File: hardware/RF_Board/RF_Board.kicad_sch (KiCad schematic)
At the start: 130 parts, among them J1 Conn_Coaxial, J2 Conn_01x04_Male, J3 Conn_Coaxial, J4 Conn_01x04_Male, J5 Conn_01x06_Female, J6 Conn_01x06_Female, J7 Conn_01x06_Female, J8 L77TSAH15SOL2RM8, Q1 2N7002, Q2 2N7002, U1 MSP430FR2355TPT, U10 QPL9096, U11 QPL9096, U12 74HC04, U13 RFM95PW, U14 TPS259573DSGR, U15 TPS259573DSGR, U2 MSP430FR2355TPT, U3 CC2500, U4 HMC574, U5 HMC574, U6 YAT-5A+, U7 SKY65900-11, U8 LFCN-2750+, U9 DEA202450BT-1213C1, Y1 Crystal_GND24, Y2 Crystal, Y3 Crystal

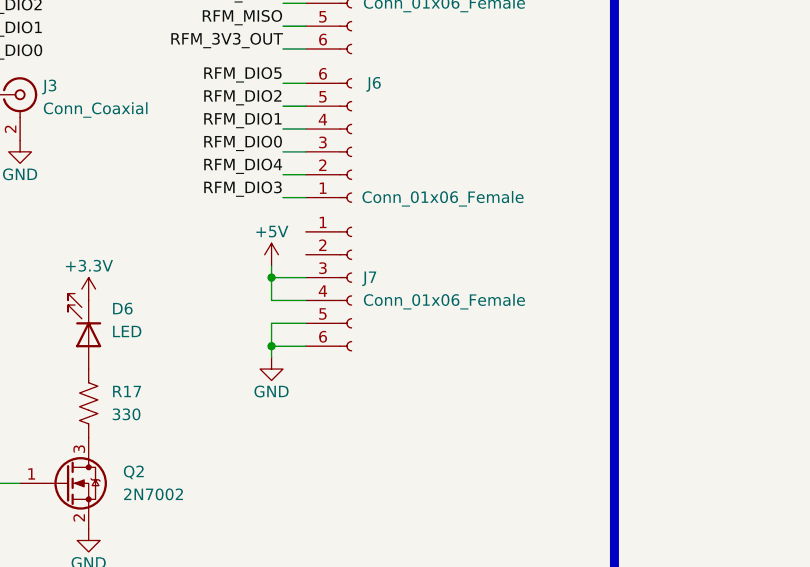
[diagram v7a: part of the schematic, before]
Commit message: start RF board digital routing
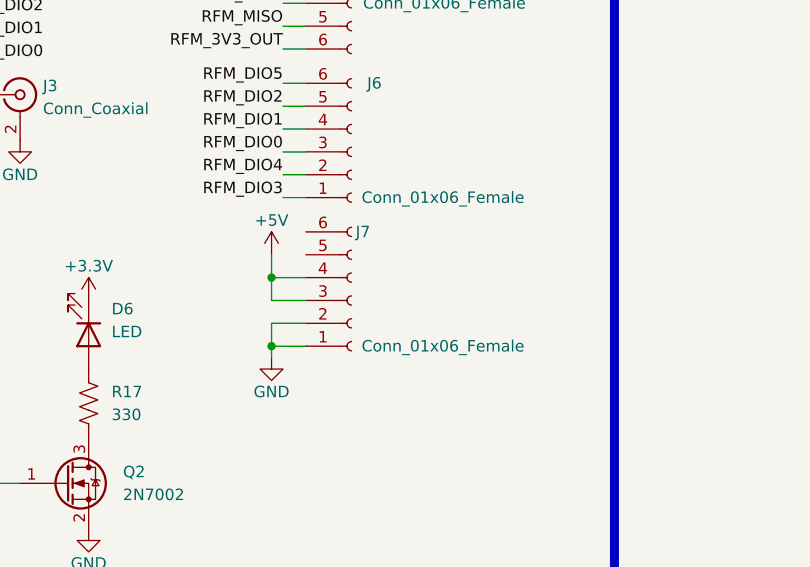
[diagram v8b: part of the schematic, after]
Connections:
- net GND: now also J7.1 (Pin_1), J7.2 (Pin_2); no longer J7.5 (Pin_5), J7.6 (Pin_6)
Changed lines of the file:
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@@
   (junction (at 537.21 74.93) (diameter 0) (color 0 0 0 0)
   )
+  (junction (at 448.31 276.86) (diameter 0) (color 0 0 0 0)
+  )
+  (junction (at 529.59 273.05) (diameter 0) (color 0 0 0 0)
+  )
+  (junction (at 252.73 107.95) (diameter 0) (color 0 0 0 0)
+  )
+  (junction (at 308.61 262.89) (diameter 0) (color 0 0 0 0)
+  )
+  (junction (at 537.21 118.11) (diameter 0) (color 0 0 0 0)
+  )
+  (junction (at 481.33 97.79) (diameter 0) (color 0 0 0 0)
+  )
+  (junction (at 410.21 226.06) (diameter 0) (color 0 0 0 0)
+  )
+  (junction (at 481.33 54.61) (diameter 0) (color 0 0 0 0)
+  )
+  (junction (at 467.36 219.71) (diameter 0) (color 0 0 0 0)
+  )
+  (junction (at 312.42 121.92) (diameter 0) (color 0 0 0 0)
+  )
+  (junction (at 297.18 269.24) (diameter 0) (color 0 0 0 0)
+  )
+  (junction (at 119.38 219.71) (diameter 0) (color 0 0 0 0)
+  )
+  (junction (at 468.63 97.79) (diameter 0) (color 0 0 0 0)
+  )
+  (junction (at 549.91 97.79) (diameter 0) (color 0 0 0 0)
+  )
+  (junction (at 549.91 54.61) (diameter 0) (color 0 0 0 0)
+  )
+  (junction (at 499.11 54.61) (diameter 0) (color 0 0 0 0)
+  )
+  (junction (at 557.53 97.79) (diameter 0) (color 0 0 0 0)
+  )
+  (junction (at 499.11 97.79) (diameter 0) (color 0 0 0 0)
+  )
+  (junction (at 529.59 250.19) (diameter 0) (color 0 0 0 0)
+  )
+  (junction (at 447.04 219.71) (diameter 0) (color 0 0 0 0)
+  )
+  (junction (at 468.63 54.61) (diameter 0) (color 0 0 0 0)
+  )
+  (junction (at 345.44 325.12) (diameter 0) (color 0 0 0 0)
+  )
+  (junction (at 256.54 245.11) (diameter 0) (color 0 0 0 0)
+  )
+  (junction (at 328.93 262.89) (diameter 0) (color 0 0 0 0)
+  )
+  (junction (at 487.68 54.61) (diameter 0) (color 0 0 0 0)
+  )
+  (junction (at 241.3 228.6) (diameter 0) (color 0 0 0 0)
+  )
+  (junction (at 435.61 251.46) (diameter 0) (color 0 0 0 0)
+  )
+  (junction (at 448.31 321.31) (diameter 0) (color 0 0 0 0)
+  )
   (junction (at 312.42 129.54) (diameter 0) (color 0 0 0 0)
-  )
-  (junction (at 448.31 276.86) (diameter 0) (color 0 0 0 0)
-  )
-  (junction (at 529.59 273.05) (diameter 0) (color 0 0 0 0)
-  )
-  (junction (at 252.73 107.95) (diameter 0) (color 0 0 0 0)
-  )
-  (junction (at 308.61 262.89) (diameter 0) (color 0 0 0 0)
-  )
-  (junction (at 537.21 118.11) (diameter 0) (color 0 0 0 0)
-  )
-  (junction (at 481.33 97.79) (diameter 0) (color 0 0 0 0)
-  )
-  (junction (at 410.21 226.06) (diameter 0) (color 0 0 0 0)
-  )
-  (junction (at 481.33 54.61) (diameter 0) (color 0 0 0 0)
-  )
-  (junction (at 467.36 219.71) (diameter 0) (color 0 0 0 0)
-  )
-  (junction (at 297.18 269.24) (diameter 0) (color 0 0 0 0)
-  )
-  (junction (at 119.38 219.71) (diameter 0) (color 0 0 0 0)
-  )
-  (junction (at 468.63 97.79) (diameter 0) (color 0 0 0 0)
-  )
-  (junction (at 549.91 97.79) (diameter 0) (color 0 0 0 0)
-  )
-  (junction (at 549.91 54.61) (diameter 0) (color 0 0 0 0)
-  )
-  (junction (at 499.11 54.61) (diameter 0) (color 0 0 0 0)
-  )
-  (junction (at 557.53 97.79) (diameter 0) (color 0 0 0 0)
-  )
-  (junction (at 499.11 97.79) (diameter 0) (color 0 0 0 0)
-  )
-  (junction (at 529.59 250.19) (diameter 0) (color 0 0 0 0)
-  )
-  (junction (at 447.04 219.71) (diameter 0) (color 0 0 0 0)
-  )
-  (junction (at 468.63 54.61) (diameter 0) (color 0 0 0 0)
-  )
-  (junction (at 345.44 325.12) (diameter 0) (color 0 0 0 0)
-  )
-  (junction (at 256.54 245.11) (diameter 0) (color 0 0 0 0)
-  )
-  (junction (at 328.93 262.89) (diameter 0) (color 0 0 0 0)
-  )
-  (junction (at 312.42 121.92) (diameter 0) (color 0 0 0 0)
-  )
-  (junction (at 487.68 54.61) (diameter 0) (color 0 0 0 0)
-  )
-  (junction (at 241.3 228.6) (diameter 0) (color 0 0 0 0)
-  )
-  (junction (at 435.61 251.46) (diameter 0) (color 0 0 0 0)
-  )
-  (junction (at 448.31 321.31) (diameter 0) (color 0 0 0 0)
   )
   (junction (at 477.52 219.71) (diameter 0) (color 0 0 0 0)
@@
     (stroke (width 0) (type default) (color 0 0 0 0))
   )
+  (wire (pts (xy 312.42 129.54) (xy 312.42 130.81))
+    (stroke (width 0) (type default) (color 0 0 0 0))
+  )
   (wire (pts (xy 447.04 321.31) (xy 448.31 321.31))
     (stroke (width 0) (type default) (color 0 0 0 0))
@@
     (stroke (width 0) (type default) (color 0 0 0 0))
   )
-  (wire (pts (xy 312.42 129.54) (xy 312.42 130.81))
-    (stroke (width 0) (type default) (color 0 0 0 0))
-  )
   (wire (pts (xy 402.59 64.77) (xy 405.13 64.77))
     (stroke (width 0) (type default) (color 0 0 0 0))
@@
   )
   (wire (pts (xy 308.61 256.54) (xy 308.61 262.89))
-    (stroke (width 0) (type default) (color 0 0 0 0))
-  )
-  (wire (pts (xy 316.23 124.46) (xy 312.42 124.46))
     (stroke (width 0) (type default) (color 0 0 0 0))
   )
@@
     (stroke (width 0) (type default) (color 0 0 0 0))
   )
-  (wire (pts (xy 312.42 121.92) (xy 312.42 120.65))
+  (wire (pts (xy 312.42 121.92) (xy 312.42 119.38))
     (stroke (width 0) (type default) (color 0 0 0 0))
   )
@@
     (stroke (width 0) (type default) (color 0 0 0 0))
   )
+  (wire (pts (xy 312.42 121.92) (xy 316.23 121.92))
+    (stroke (width 0) (type default) (color 0 0 0 0))
+  )
   (wire (pts (xy 190.5 254) (xy 193.04 254))
     (stroke (width 0) (type default) (color 0 0 0 0))
@@
   )
   (wire (pts (xy 41.91 113.03) (xy 44.45 113.03))
-    (stroke (width 0) (type default) (color 0 0 0 0))
-  )
-  (wire (pts (xy 312.42 129.54) (xy 316.23 129.54))
     (stroke (width 0) (type default) (color 0 0 0 0))
   )
@@
     (stroke (width 1) (type default) (color 0 0 0 0))
   )
-  (wire (pts (xy 316.23 127) (xy 312.42 127))
-    (stroke (width 0) (type default) (color 0 0 0 0))
-  )
   (wire (pts (xy 459.74 309.88) (xy 461.01 309.88))
     (stroke (width 0) (type default) (color 0 0 0 0))
@@
     (stroke (width 0) (type default) (color 0 0 0 0))
   )
+  (wire (pts (xy 312.42 127) (xy 316.23 127))
+    (stroke (width 0) (type default) (color 0 0 0 0))
+  )
   (wire (pts (xy 430.53 54.61) (xy 433.07 54.61))
     (stroke (width 0) (type default) (color 0 0 0 0))
@@
     (stroke (width 0) (type default) (color 0 0 0 0))
   )
+  (wire (pts (xy 312.42 129.54) (xy 316.23 129.54))
+    (stroke (width 0) (type default) (color 0 0 0 0))
+  )
   (wire (pts (xy 402.59 67.31) (xy 405.13 67.31))
     (stroke (width 0) (type default) (color 0 0 0 0))
@@
     (stroke (width 0) (type default) (color 0 0 0 0))
   )
+  (wire (pts (xy 312.42 124.46) (xy 316.23 124.46))
+    (stroke (width 0) (type default) (color 0 0 0 0))
+  )
   (wire (pts (xy 481.33 55.88) (xy 481.33 54.61))
     (stroke (width 0) (type default) (color 0 0 0 0))
@@
   )
   (wire (pts (xy 351.79 245.11) (xy 354.33 245.11))
-    (stroke (width 0) (type default) (color 0 0 0 0))
-  )
-  (wire (pts (xy 312.42 121.92) (xy 316.23 121.92))
     (stroke (width 0) (type default) (color 0 0 0 0))
   )
@@
     (pin "1")
   )
-  (symbol (lib_id "RF_Board_Symbols:Conn_01x06_Female") (at 321.31 121.92 0) (unit 1)
-    (in_bom yes) (on_board yes) (fields_autoplaced)
-    (property "Reference" "J7" (id 0) (at 322.58 121.9199 0)
-      (effects (font (size 1.27 1.27)) (justify left))
-    )
-    (property "Value" "Conn_01x06_Female" (id 1) (at 322.58 124.4599 0)
-      (effects (font (size 1.27 1.27)) (justify left))
-    )
-    (property "Footprint" "RF_Board_Footprints:PinHeader_1x06_P2.54mm_Vertical" (id 2) (at 321.31 121.92 0)
-      (effects (font (size 1.27 1.27)) hide)
-    )
-    (property "Datasheet" "~" (id 3) (at 321.31 121.92 0)
+  (symbol (lib_id "RF_Board_Symbols:Conn_01x06_Female") (at 321.31 124.46 0) (mirror x) (unit 1)
+    (in_bom yes) (on_board yes)
+    (property "Reference" "J7" (id 0) (at 322.58 116.84 0))
+    (property "Value" "Conn_01x06_Female" (id 1) (at 331.47 129.54 0))
+    (property "Footprint" "RF_Board_Footprints:PinHeader_1x06_P2.54mm_Vertical" (id 2) (at 321.31 124.46 0)
+      (effects (font (size 1.27 1.27)) hide)
+    )
+    (property "Datasheet" "~" (id 3) (at 321.31 124.46 0)
       (effects (font (size 1.27 1.27)) hide)
     )
@@
     (pin "1")
   )
-  (symbol (lib_id "power:+5V") (at 312.42 120.65 0) (unit 1)
-    (in_bom yes) (on_board yes)
-    (property "Reference" "#PWR062" (id 0) (at 312.42 124.46 0)
-      (effects (font (size 1.27 1.27)) hide)
-    )
-    (property "Value" "+5V" (id 1) (at 312.42 116.84 0))
-    (property "Footprint" "" (id 2) (at 312.42 120.65 0)
-      (effects (font (size 1.27 1.27)) hide)
-    )
-    (property "Datasheet" "" (id 3) (at 312.42 120.65 0)
-      (effects (font (size 1.27 1.27)) hide)
-    )
+  (symbol (lib_id "power:+5V") (at 312.42 119.38 0) (unit 1)
+    (in_bom yes) (on_board yes)
+    (property "Reference" "#PWR062" (id 0) (at 312.42 123.19 0)
+      (effects (font (size 1.27 1.27)) hide)
+    )
+    (property "Value" "+5V" (id 1) (at 312.42 115.57 0))
+    (property "Footprint" "" (id 2) (at 312.42 119.38 0)
+      (effects (font (size 1.27 1.27)) hide)
+    )
+    (property "Datasheet" "" (id 3) (at 312.42 119.38 0)
+      (effects (font (size 1.27 1.27)) hide)
+    )
